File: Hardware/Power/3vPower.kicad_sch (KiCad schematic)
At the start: 27 parts, among them U11 74AHC1G00, U8 MAX17643, U9 MAX17643

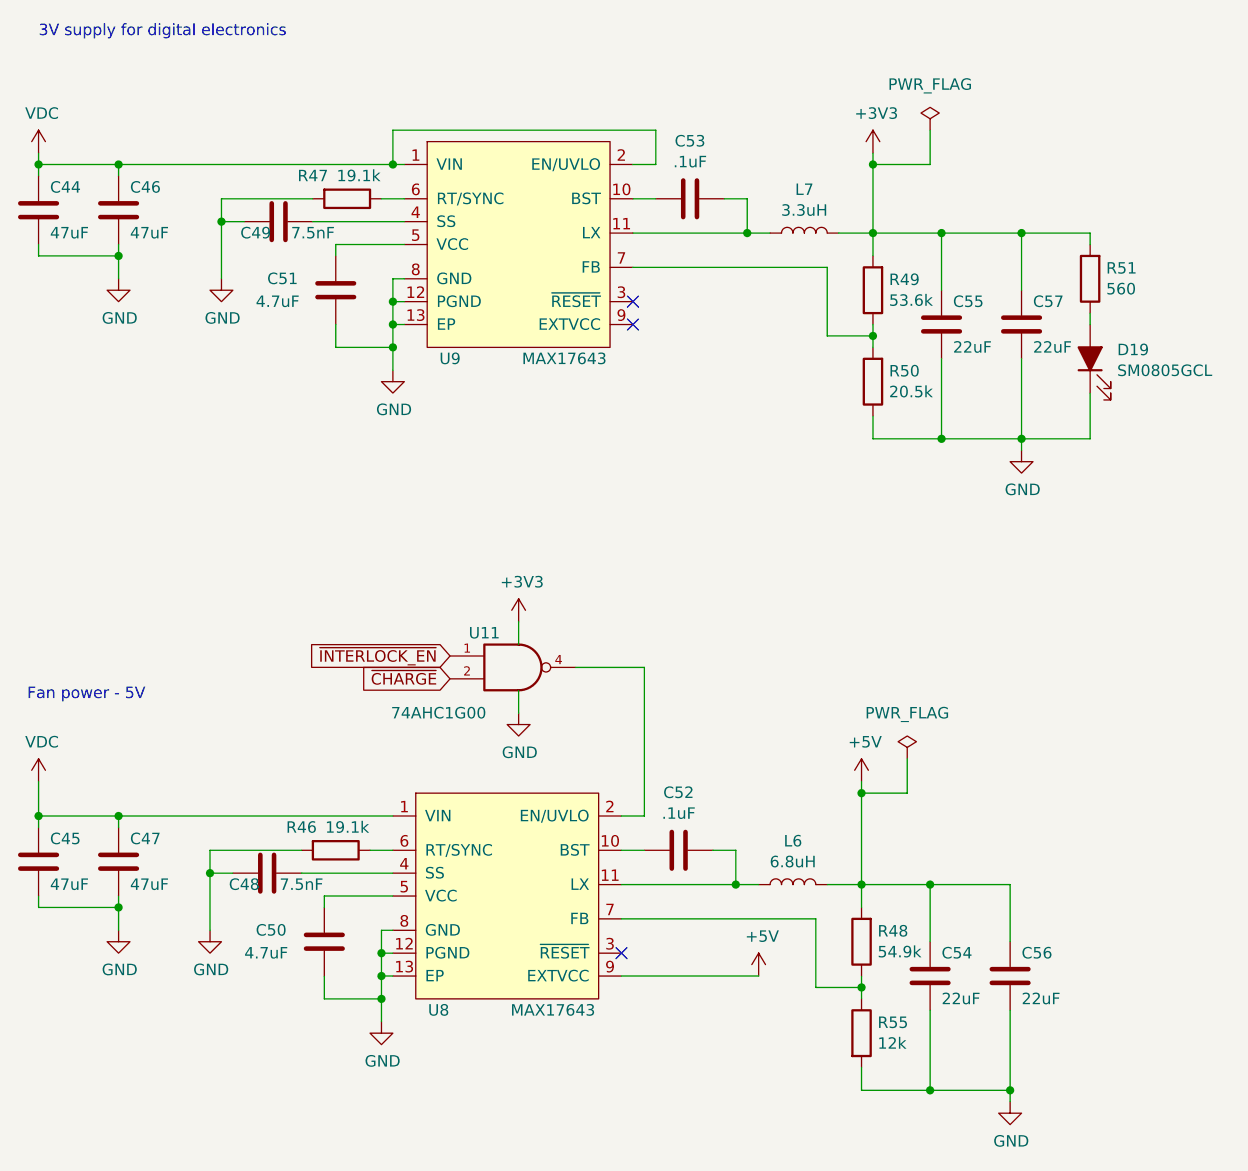
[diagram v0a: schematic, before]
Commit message: Update to kicad 8
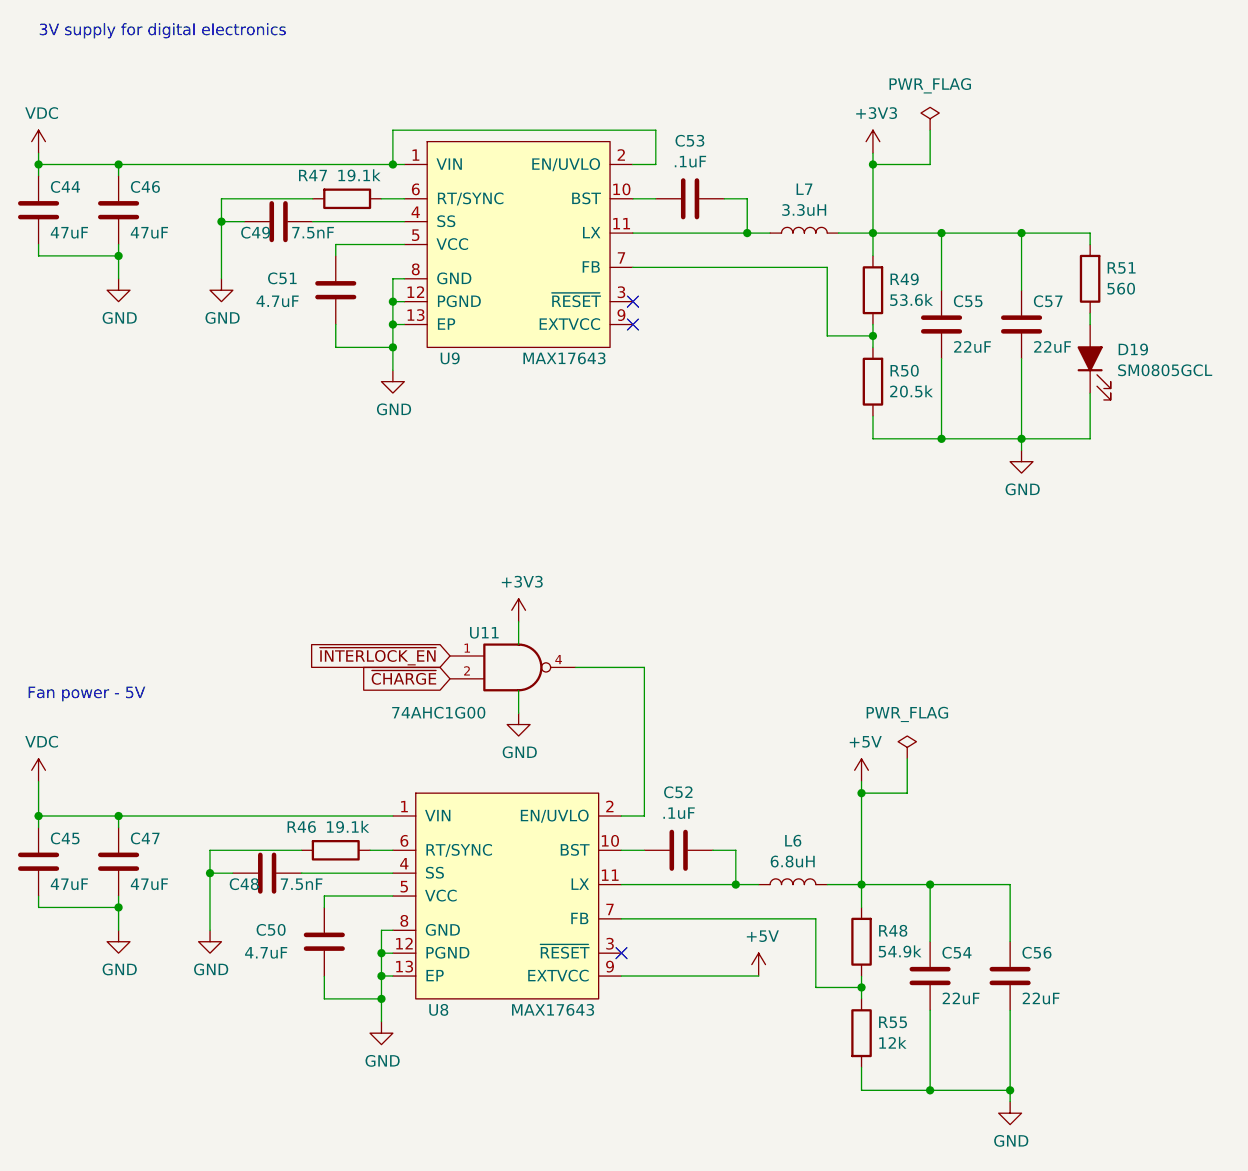
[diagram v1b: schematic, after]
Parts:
- D19: footprint LED_SMD:LED_0805_2012Metric_Castellated -> LED_SMD:LED_0805_2012Metric
